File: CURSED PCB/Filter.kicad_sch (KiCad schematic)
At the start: 4 parts, among them U10 OPA2314AIDR, U9 OPA2314AIDR

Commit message: Updates to PCB before exam sesaon
idk what I added ngl
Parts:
- removed U10, U9: OPA2314AIDR, PCM_Package_TO_SOT_SMD_AKL:SOT-23-5, symbol PCM_Amplifier_Operational_AKL:OPA313IDBV
- added C5: C_Small, symbol Device:C_Small
- added R10: 51kΩ, symbol Device:R_US
- added U9: OPAMP_5-pin_Generic, Package_TO_SOT_SMD:SOT-23-5, symbol PCM_Amplifier_Operational_AKL:OPAMP_5-pin_Generic
- R9: value R_US -> 51kΩ
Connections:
- net +5V: now also U9.5 (V+)
- net GND: now also U9.2 (V-)
- net VOUT: now also C5.2, U9.1, U9.4 (-)
- net at R9.2: now also C5.1, R10.1; no longer C18.1
- new net: C18.1, R10.2, U9.3 (+)
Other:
- note added: "Reference sheet: https://ez.analog.com/cfs-file/__key/communityserver-wikis-components-files/00-00-00-06-97/KWIK_5F00_FAQ-_2D00_-Design-of-an-anti_2D00_aliasing-Sallen_2D00_Key"
- note removed: "Reference sheet: https://www.ti.com/lit/an/slyt626/slyt626.pdf?ts=1763997895234&ref_url=https%253A%252F%252Fwww.google.com%252F"
- moved on the sheet: C18, R9

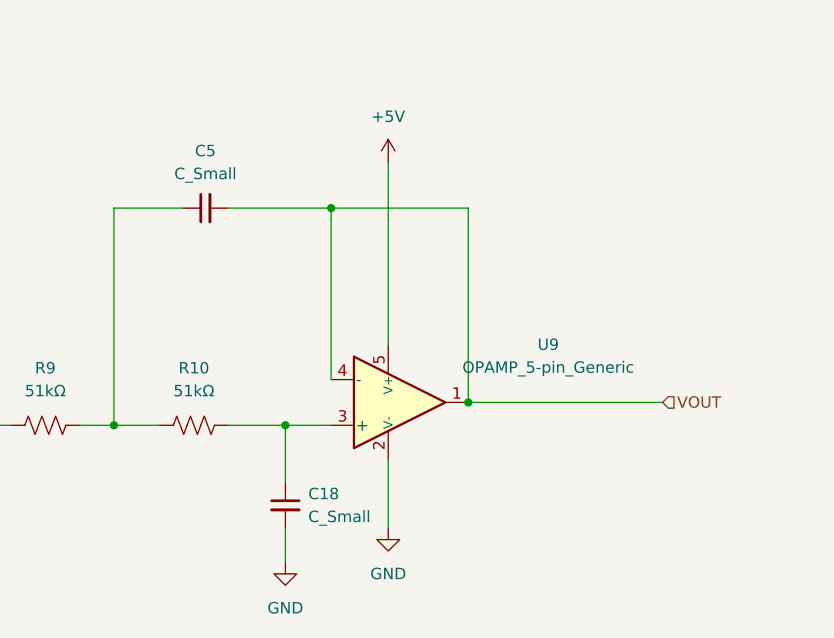
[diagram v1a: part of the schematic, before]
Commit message: Added values for schematic
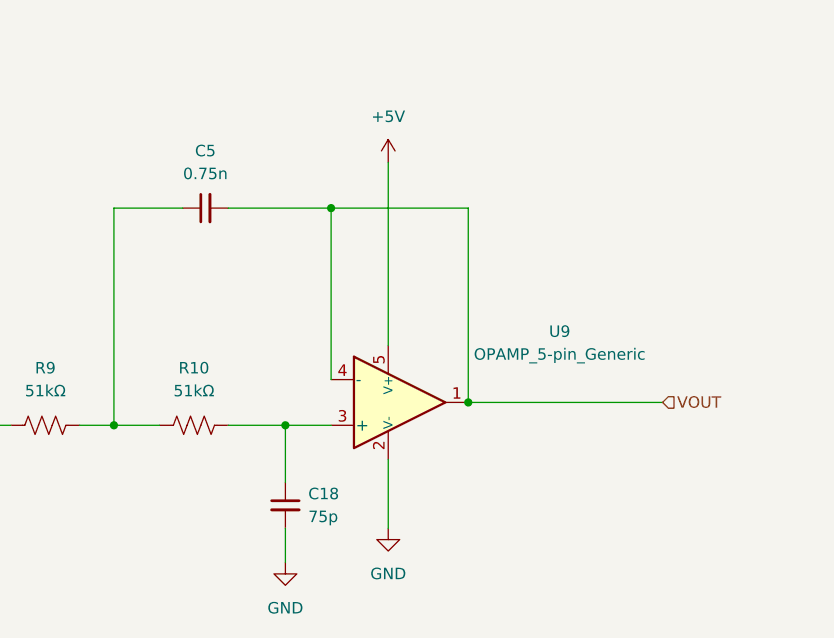
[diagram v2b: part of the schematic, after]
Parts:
- C18: value C_Small -> 75p
- C5: value C_Small -> 0.75n
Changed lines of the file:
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@@
 			)
 		)
-		(property "Value" "C_Small"
+		(property "Value" "0.75n"
 			(at 82.5563 72.39 90)
 			(effects
@@
 			)
 		)
-		(property "Value" "C_Small"
+		(property "Value" "75p"
 			(at 93.98 110.4962 0)
 			(effects
@@
 		(dnp no)
 		(property "Reference" "U9"
-			(at 120.65 91.3698 0)
+			(at 121.92 89.916 0)
 			(effects
 				(font
@@
 		)
 		(property "Value" "OPAMP_5-pin_Generic"
-			(at 120.65 93.9098 0)
-			(effects
-				(font
+			(at 121.92 92.456 0)
+			(effects
+				(font

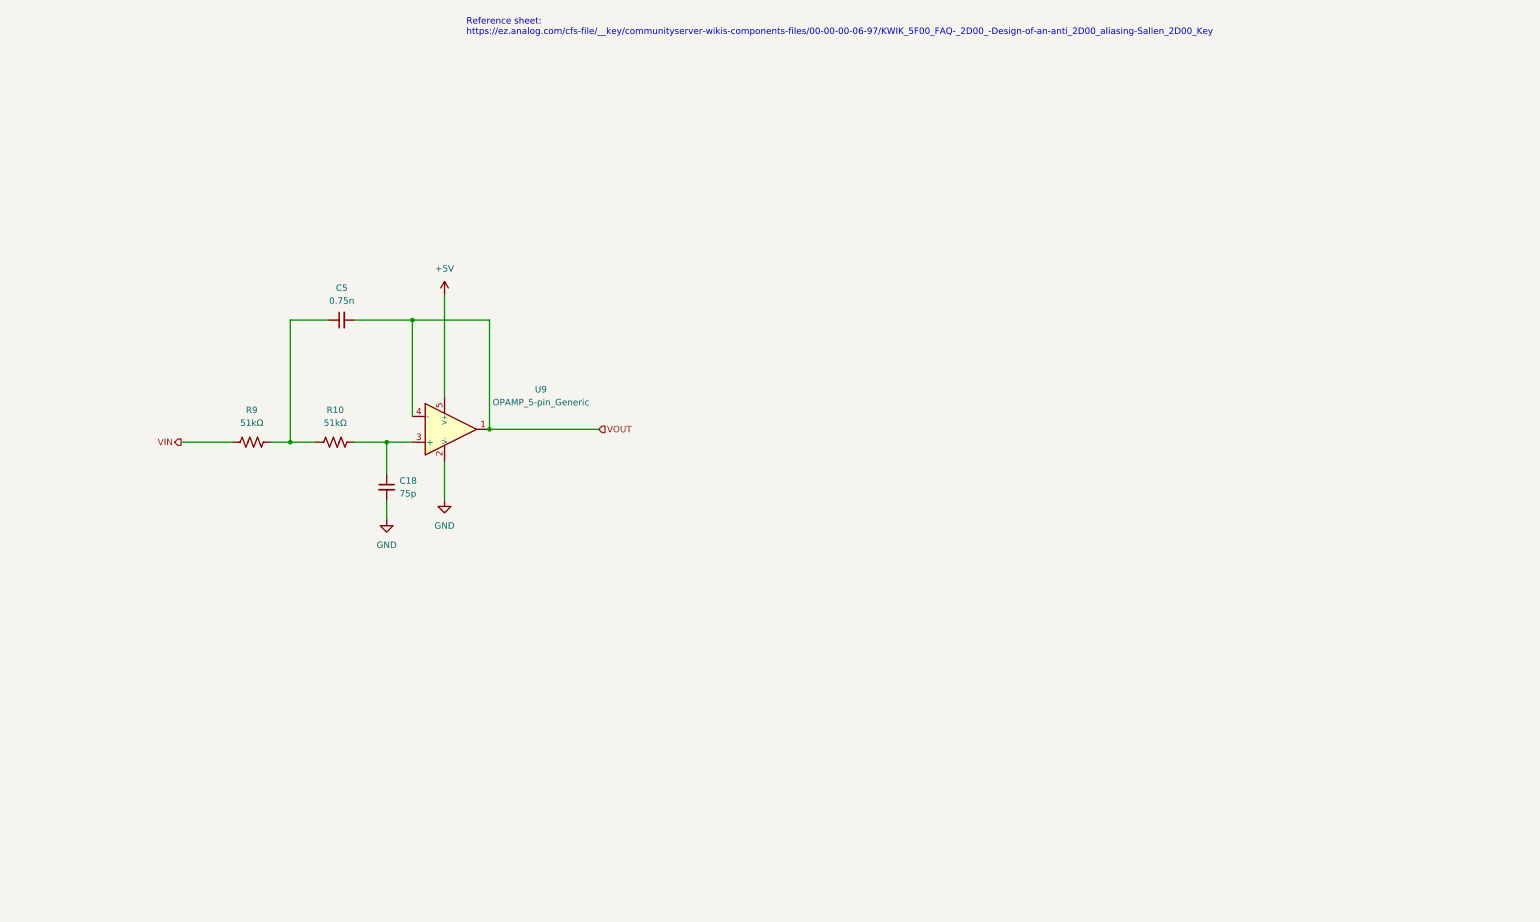
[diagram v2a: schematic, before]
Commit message: Added reference voltage and some other stuff
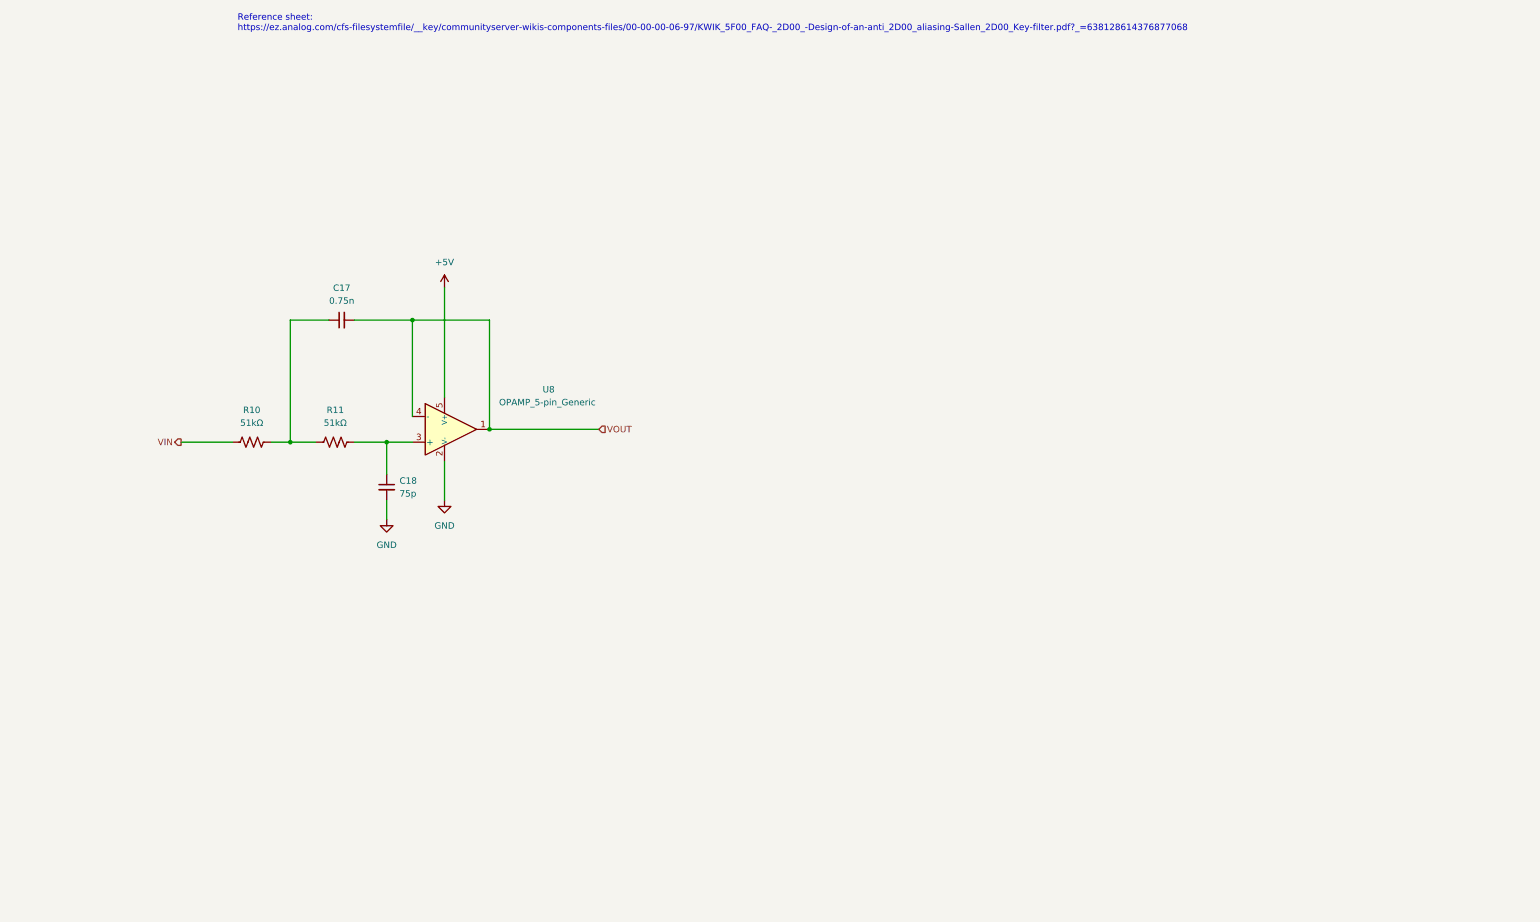
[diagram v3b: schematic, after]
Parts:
- C17: renamed from C5; footprint (none) -> Capacitor_SMD:C_0201_0603Metric
- C18: footprint (none) -> Capacitor_SMD:C_0201_0603Metric
- R10: renamed from R9; footprint (none) -> Resistor_SMD:R_0201_0603Metric
- R11: renamed from R10; footprint (none) -> Resistor_SMD:R_0201_0603Metric
- renumbered U9 to U8
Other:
- note added: "Reference sheet: https://ez.analog.com/cfs-filesystemfile/__key/communityserver-wikis-components-files/00-00-00-06-97/KWIK_5F00_FAQ-_2D00_-Design-of-an-anti_2D00_aliasing-Sallen_2D00_Key-filter.pdf?_=638128614376877068"
- note removed: "Reference sheet: https://ez.analog.com/cfs-file/__key/communityserver-wikis-components-files/00-00-00-06-97/KWIK_5F00_FAQ-_2D00_-Design-of-an-anti_2D00_aliasing-Sallen_2D00_Key"
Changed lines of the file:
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@@
 	(generator_version "9.0")
 	(paper "A4")
-	(text "Reference sheet:\nhttps://ez.analog.com/cfs-file/__key/communityserver-wikis-components-files/00-00-00-06-97/KWIK_5F00_FAQ-_2D00_-Design-of-an-anti_2D00_aliasing-Sallen_2D00_Key"
-		(exclude_from_sim no)
-		(at 107.188 18.288 0)
+	(text "Reference sheet:\nhttps://ez.analog.com/cfs-filesystemfile/__key/communityserver-wikis-components-files/00-00-00-06-97/KWIK_5F00_FAQ-_2D00_-Design-of-an-anti_2D00_aliasing-Sallen_2D00_Key-filter.pdf?_=638128614376877068"
+		(exclude_from_sim no)
+		(at 61.976 17.526 0)
 		(effects
 			(font
@@
 	(wire
 		(pts
-			(xy 102.87 71.12) (xy 102.87 91.44)
+			(xy 102.87 69.85) (xy 102.87 91.44)
 		)
 		(stroke
@@
 		(on_board yes)
 		(dnp no)
-		(property "Reference" "#PWR047"
+		(property "Reference" "#PWR045"
 			(at 91.44 121.92 0)
 			(effects
@@
 			(project ""
 				(path "/9fb1a86f-679c-4b88-9ed1-932f4f414580/543706d6-8cb0-4c51-81f6-888765ec3907/1dbad184-dd5f-4b28-bd02-77889e07b3d7"
-					(reference "#PWR047")
+					(reference "#PWR045")
 					(unit 1)
 				)
@@
 		(dnp no)
 		(fields_autoplaced yes)
-		(property "Reference" "C5"
+		(property "Reference" "C17"
 			(at 82.5563 69.85 90)
 			(effects
@@
 			)
 		)
-		(property "Footprint" ""
+		(property "Footprint" "Capacitor_SMD:C_0201_0603Metric"
 			(at 82.55 76.2 0)
 			(effects
@@
 			(project "sensor_1"
 				(path "/9fb1a86f-679c-4b88-9ed1-932f4f414580/543706d6-8cb0-4c51-81f6-888765ec3907/1dbad184-dd5f-4b28-bd02-77889e07b3d7"
-					(reference "C5")
+					(reference "C17")
 					(unit 1)
 				)
@@
 			)
 		)
-		(property "Footprint" ""
+		(property "Footprint" "Capacitor_SMD:C_0201_0603Metric"
 			(at 91.44 109.22 0)
 			(effects
@@
 		(on_board yes)
 		(dnp no)
-		(property "Reference" "#PWR046"
+		(property "Reference" "#PWR047"
 			(at 102.87 118.11 0)
 			(effects
@@
 			(project "sensor_1"
 				(path "/9fb1a86f-679c-4b88-9ed1-932f4f414580/543706d6-8cb0-4c51-81f6-888765ec3907/1dbad184-dd5f-4b28-bd02-77889e07b3d7"
-					(reference "#PWR046")
+					(reference "#PWR047")
 					(unit 1)
 				)
@@
 	(symbol
 		(lib_id "power:+5V")
-		(at 102.87 71.12 0)
+		(at 102.87 69.85 0)
 		(unit 1)
 		(exclude_from_sim no)
@@
 		(dnp no)
 		(fields_autoplaced yes)
-		(property "Reference" "#PWR045"
-			(at 102.87 74.93 0)
+		(property "Reference" "#PWR046"
+			(at 102.87 73.66 0)
 			(effects
 				(font
@@
 		)
 		(property "Value" "+5V"
-			(at 102.87 66.04 0)
+			(at 102.87 64.77 0)
 			(effects
 				(font
@@
 		)
 		(property "Footprint" ""
-			(at 102.87 71.12 0)
+			(at 102.87 69.85 0)
 			(effects
 				(font
@@
 		)
 		(property "Datasheet" ""
-			(at 102.87 71.12 0)
+			(at 102.87 69.85 0)
 			(effects
 				(font
@@
 		)
 		(property "Description" "Power symbol creates a global label with name \"+5V\""
-			(at 102.87 71.12 0)
+			(at 102.87 69.85 0)
 			(effects
 				(font
@@
 			(project ""
 				(path "/9fb1a86f-679c-4b88-9ed1-932f4f414580/543706d6-8cb0-4c51-81f6-888765ec3907/1dbad184-dd5f-4b28-bd02-77889e07b3d7"
-					(reference "#PWR045")
+					(reference "#PWR046")
 					(unit 1)
 				)
@@
 		(lib_id "Device:R_US")
 		(at 64.77 100.33 90)
-		(unit 1)
-		(exclude_from_sim no)
-		(in_bom yes)
-		(on_board yes)
-		(dnp no)
-		(fields_autoplaced yes)
-		(property "Reference" "R9"
-			(at 64.77 93.98 90)
-			(effects
-				(font
-					(size 1.27 1.27)
-				)
-			)
-		)
-		(property "Value" "51kΩ"
-			(at 64.77 96.52 90)
-			(effects
-				(font
-					(size 1.27 1.27)
-				)
-			)
-		)
-		(property "Footprint" ""
-			(at 65.024 99.314 90)
-			(effects
-				(font
-					(size 1.27 1.27)
-				)
-				(hide yes)
-			)
-		)
-		(property "Datasheet" "~"
-			(at 64.77 100.33 0)
-			(effects
-				(font
-					(size 1.27 1.27)
-				)
-				(hide yes)
-			)
-		)
-		(property "Description" "Resistor, US symbol"
-			(at 64.77 100.33 0)
-			(effects
-				(font
-					(size 1.27 1.27)
-				)
-				(hide yes)
-			)
-		)
-		(pin "2"
-		)
-		(pin "1"
-		)
-		(instances
-			(project ""
-				(path "/9fb1a86f-679c-4b88-9ed1-932f4f414580/543706d6-8cb0-4c51-81f6-888765ec3907/1dbad184-dd5f-4b28-bd02-77889e07b3d7"
-					(reference "R9")
-					(unit 1)
-				)
-			)
-		)
-	)
-	(symbol
-		(lib_id "Device:R_US")
-		(at 81.28 100.33 90)
 		(unit 1)
 		(exclude_from_sim no)
@@
 		(fields_autoplaced yes)
 		(property "Reference" "R10"
+			(at 64.77 93.98 90)
+			(effects
+				(font
+					(size 1.27 1.27)
+				)
+			)
+		)
+		(property "Value" "51kΩ"
+			(at 64.77 96.52 90)
+			(effects
+				(font
+					(size 1.27 1.27)
+				)
+			)
+		)
+		(property "Footprint" "Resistor_SMD:R_0201_0603Metric"
+			(at 65.024 99.314 90)
+			(effects
+				(font
+					(size 1.27 1.27)
+				)
+				(hide yes)
+			)
+		)
+		(property "Datasheet" "~"
+			(at 64.77 100.33 0)
+			(effects
+				(font
+					(size 1.27 1.27)
+				)
+				(hide yes)
+			)
+		)
+		(property "Description" "Resistor, US symbol"
+			(at 64.77 100.33 0)
+			(effects
+				(font
+					(size 1.27 1.27)
+				)
+				(hide yes)
+			)
+		)
+		(pin "2"
+		)
+		(pin "1"
+		)
+		(instances
+			(project ""
+				(path "/9fb1a86f-679c-4b88-9ed1-932f4f414580/543706d6-8cb0-4c51-81f6-888765ec3907/1dbad184-dd5f-4b28-bd02-77889e07b3d7"
+					(reference "R10")
+					(unit 1)
+				)
+			)
+		)
+	)
+	(symbol
+		(lib_id "Device:R_US")
+		(at 81.28 100.33 90)
+		(unit 1)
+		(exclude_from_sim no)
+		(in_bom yes)
+		(on_board yes)
+		(dnp no)
+		(fields_autoplaced yes)
+		(property "Reference" "R11"
 			(at 81.28 93.98 90)
 			(effects
@@
 			)
 		)
-		(property "Footprint" ""
+		(property "Footprint" "Resistor_SMD:R_0201_0603Metric"
 			(at 81.534 99.314 90)
 			(effects
@@
 			(project "sensor_1"
 				(path "/9fb1a86f-679c-4b88-9ed1-932f4f414580/543706d6-8cb0-4c51-81f6-888765ec3907/1dbad184-dd5f-4b28-bd02-77889e07b3d7"
-					(reference "R10")
+					(reference "R11")
 					(unit 1)
 				)
@@
 		(on_board yes)
 		(dnp no)
-		(property "Reference" "U9"
-			(at 121.92 89.916 0)
+		(property "Reference" "U8"
+			(at 123.444 89.916 0)
 			(effects
 				(font
@@
 		)
 		(property "Value" "OPAMP_5-pin_Generic"
-			(at 121.92 92.456 0)
+			(at 123.19 92.456 0)
 			(effects
 				(font
@@
 			(project ""
 				(path "/9fb1a86f-679c-4b88-9ed1-932f4f414580/543706d6-8cb0-4c51-81f6-888765ec3907/1dbad184-dd5f-4b28-bd02-77889e07b3d7"
-					(reference "U9")
+					(reference "U8")
 					(unit 1)
 				)

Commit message: Changes to stuff
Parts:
- C17: value 0.75n -> 1u
- C18: value 75p -> 1u
- R10: value 51kΩ -> 11.7k
- R11: value 51kΩ -> 21k
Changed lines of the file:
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@@
+	)
+	(junction
+		(at 111.76 86.36)
+		(diameter 0)
+		(color 0 0 0 0)
 	)
 	(junction
@@
 	)
 	(junction
-		(at 96.52 76.2)
-		(diameter 0)
-		(color 0 0 0 0)
-	)
-	(junction
 		(at 91.44 100.33)
 		(diameter 0)
@@
 	(wire
 		(pts
+			(xy 96.52 95.25) (xy 96.52 86.36)
+		)
+		(stroke
+			(width 0)
+			(type default)
+		)
+	)
+	(wire
+		(pts
+			(xy 96.52 86.36) (xy 111.76 86.36)
+		)
+		(stroke
+			(width 0)
+			(type default)
+		)
+	)
+	(wire
+		(pts
 			(xy 91.44 100.33) (xy 91.44 106.68)
 		)
@@
 	(wire
 		(pts
-			(xy 96.52 76.2) (xy 111.76 76.2)
-		)
-		(stroke
-			(width 0)
-			(type default)
-		)
-	)
-	(wire
-		(pts
-			(xy 85.09 76.2) (xy 96.52 76.2)
+			(xy 111.76 86.36) (xy 111.76 97.79)
+		)
+		(stroke
+			(width 0)
+			(type default)
+		)
+	)
+	(wire
+		(pts
+			(xy 85.09 76.2) (xy 111.76 76.2)
 		)
 		(stroke
@@
 	(wire
 		(pts
-			(xy 111.76 76.2) (xy 111.76 97.79)
+			(xy 111.76 76.2) (xy 111.76 86.36)
 		)
 		(stroke
@@
 		(pts
 			(xy 80.01 76.2) (xy 72.39 76.2)
-		)
-		(stroke
-			(width 0)
-			(type default)
-		)
-	)
-	(wire
-		(pts
-			(xy 96.52 76.2) (xy 96.52 95.25)
 		)
 		(stroke
@@
 			)
 		)
-		(property "Value" "0.75n"
+		(property "Value" "1u"
 			(at 82.5563 72.39 90)
 			(effects
@@
 			)
 		)
-		(property "Value" "75p"
+		(property "Value" "1u"
 			(at 93.98 110.4962 0)
 			(effects
@@
 			)
 		)
-		(property "Value" "51kΩ"
+		(property "Value" "11.7k"
 			(at 64.77 96.52 90)
 			(effects
@@
 			)
 		)
-		(property "Value" "51kΩ"
+		(property "Value" "21k"
 			(at 81.28 96.52 90)
 			(effects

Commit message: file
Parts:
- C17, C18: footprint Capacitor_SMD:C_0201_0603Metric -> Capacitor_SMD:C_0603_1608Metric_Pad1.08x0.95mm_HandSolder
- R10, R11: footprint Resistor_SMD:R_0201_0603Metric -> Resistor_SMD:R_0603_1608Metric_Pad0.98x0.95mm_HandSolder
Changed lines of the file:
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@@
 			)
 		)
-		(property "Footprint" "Capacitor_SMD:C_0201_0603Metric"
+		(property "Footprint" "Capacitor_SMD:C_0603_1608Metric_Pad1.08x0.95mm_HandSolder"
 			(at 82.55 76.2 0)
 			(effects
@@
 			)
 		)
-		(property "Footprint" "Capacitor_SMD:C_0201_0603Metric"
+		(property "Footprint" "Capacitor_SMD:C_0603_1608Metric_Pad1.08x0.95mm_HandSolder"
 			(at 91.44 109.22 0)
 			(effects
@@
 			)
 		)
-		(property "Footprint" "Resistor_SMD:R_0201_0603Metric"
+		(property "Footprint" "Resistor_SMD:R_0603_1608Metric_Pad0.98x0.95mm_HandSolder"
 			(at 65.024 99.314 90)
 			(effects
@@
 			)
 		)
-		(property "Footprint" "Resistor_SMD:R_0201_0603Metric"
+		(property "Footprint" "Resistor_SMD:R_0603_1608Metric_Pad0.98x0.95mm_HandSolder"
 			(at 81.534 99.314 90)
 			(effects

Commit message: name
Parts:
- U8: value OPAMP_5-pin_Generic -> LTC2066
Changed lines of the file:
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@@
 			)
 		)
-		(property "Value" "OPAMP_5-pin_Generic"
+		(property "Value" "LTC2066"
 			(at 123.19 92.456 0)
 			(effects

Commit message: redone pcb
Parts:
- C17, C18: footprint Capacitor_SMD:C_0603_1608Metric_Pad1.08x0.95mm_HandSolder -> Capacitor_SMD:C_0805_2012Metric_Pad1.18x1.45mm_HandSolder
- R10, R11: footprint Resistor_SMD:R_0603_1608Metric_Pad0.98x0.95mm_HandSolder -> Resistor_SMD:R_0805_2012Metric_Pad1.20x1.40mm_HandSolder
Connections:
- net GND renamed AGND
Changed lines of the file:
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@@
 			)
 		)
-		(property "Value" "GND"
+		(property "Value" "AGND"
 			(at 91.44 120.65 0)
 			(effects
@@
 			)
 		)
-		(property "Footprint" "Capacitor_SMD:C_0603_1608Metric_Pad1.08x0.95mm_HandSolder"
+		(property "Footprint" "Capacitor_SMD:C_0805_2012Metric_Pad1.18x1.45mm_HandSolder"
 			(at 82.55 76.2 0)
 			(effects
@@
 			)
 		)
-		(property "Footprint" "Capacitor_SMD:C_0603_1608Metric_Pad1.08x0.95mm_HandSolder"
+		(property "Footprint" "Capacitor_SMD:C_0805_2012Metric_Pad1.18x1.45mm_HandSolder"
 			(at 91.44 109.22 0)
 			(effects
@@
 			)
 		)
-		(property "Value" "GND"
+		(property "Value" "AGND"
 			(at 102.87 116.84 0)
 			(effects
@@
 			)
 		)
-		(property "Footprint" "Resistor_SMD:R_0603_1608Metric_Pad0.98x0.95mm_HandSolder"
+		(property "Footprint" "Resistor_SMD:R_0805_2012Metric_Pad1.20x1.40mm_HandSolder"
 			(at 65.024 99.314 90)
 			(effects
@@
 			)
 		)
-		(property "Footprint" "Resistor_SMD:R_0603_1608Metric_Pad0.98x0.95mm_HandSolder"
+		(property "Footprint" "Resistor_SMD:R_0805_2012Metric_Pad1.20x1.40mm_HandSolder"
 			(at 81.534 99.314 90)
 			(effects

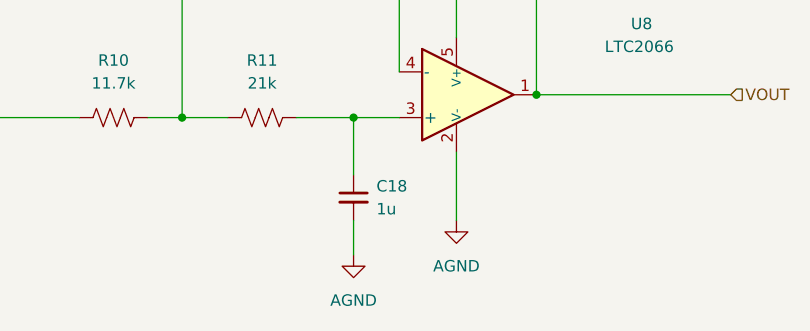
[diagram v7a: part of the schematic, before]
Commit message: no spilt-ground plane (bad idea)
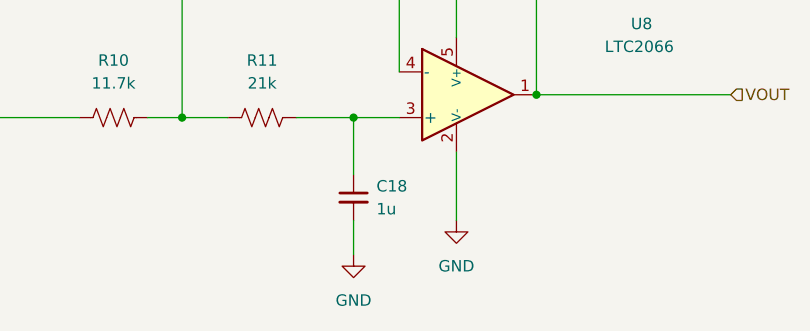
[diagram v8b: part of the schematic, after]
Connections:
- net AGND renamed GND
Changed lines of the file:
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@@
 			)
 		)
-		(property "Value" "AGND"
+		(property "Value" "GND"
 			(at 91.44 120.65 0)
 			(effects
@@
 			)
 		)
-		(property "Value" "AGND"
+		(property "Value" "GND"
 			(at 102.87 116.84 0)
 			(effects
